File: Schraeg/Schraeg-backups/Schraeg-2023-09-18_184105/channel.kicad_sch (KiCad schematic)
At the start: 51 parts, among them U1 TL074, U2 TL074, U3 V2164, U4 TL074, U6 TL074

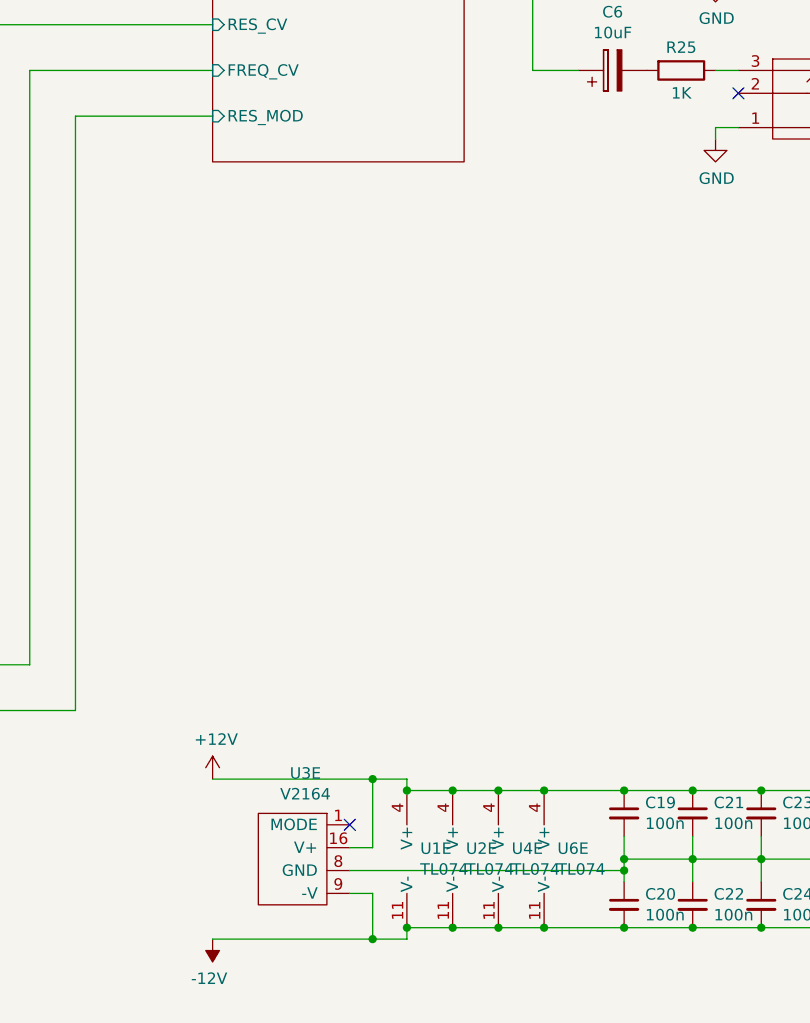
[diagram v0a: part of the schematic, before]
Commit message: fixes filter schematic
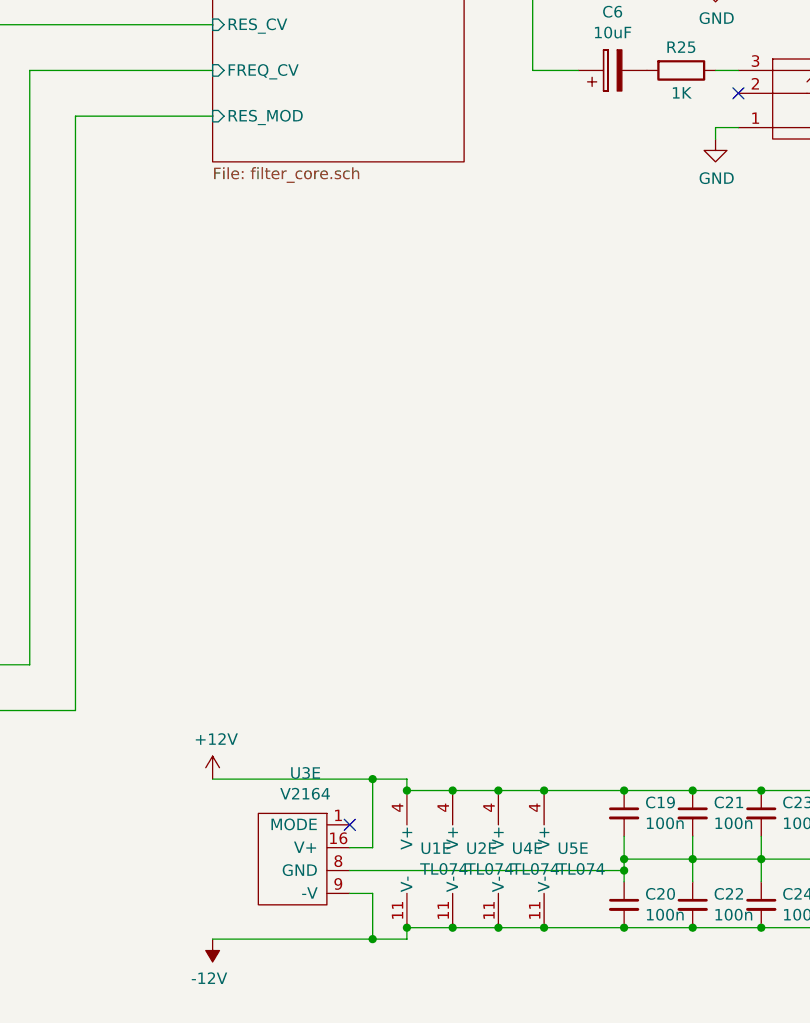
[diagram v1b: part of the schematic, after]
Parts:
- renumbered U6 to U5
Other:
- sheet Filter Core: file filter_core.kicad_sch -> filter_core.sch
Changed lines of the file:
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@@
   (symbol (lib_id "Device:C_Small") (at 110.49 107.95 0) (unit 1)
     (in_bom yes) (on_board yes) (dnp no)
-    (property "Reference" "C1" (at 112.8268 106.7816 0)
+    (property "Reference" "C?" (at 112.8268 106.7816 0)
       (effects (font (size 1.27 1.27)) (justify left))
     )
@@
   (symbol (lib_id "power:GND") (at 133.35 88.9 0) (unit 1)
     (in_bom yes) (on_board yes) (dnp no)
-    (property "Reference" "#PWR015" (at 133.35 95.25 0)
+    (property "Reference" "#PWR?" (at 133.35 95.25 0)
       (effects (font (size 1.27 1.27)) hide)
     )
@@
   (symbol (lib_id "power:GND") (at 110.49 110.49 0) (unit 1)
     (in_bom yes) (on_board yes) (dnp no)
-    (property "Reference" "#PWR013" (at 110.49 116.84 0)
+    (property "Reference" "#PWR?" (at 110.49 116.84 0)
       (effects (font (size 1.27 1.27)) hide)
     )
@@
   (symbol (lib_id "Schraeg-rescue:V2164-v2164") (at 120.65 97.79 0) (mirror x) (unit 1)
     (in_bom yes) (on_board yes) (dnp no)
-    (property "Reference" "U3" (at 121.285 89.789 0)
+    (property "Reference" "U?" (at 121.285 89.789 0)
       (effects (font (size 1.27 1.27)))
     )
@@
   (symbol (lib_id "power:GND") (at 110.49 77.47 180) (unit 1)
     (in_bom yes) (on_board yes) (dnp no)
-    (property "Reference" "#PWR012" (at 110.49 71.12 0)
+    (property "Reference" "#PWR?" (at 110.49 71.12 0)
       (effects (font (size 1.27 1.27)) hide)
     )
@@
   (symbol (lib_id "power:GND") (at 274.32 153.67 0) (unit 1)
     (in_bom yes) (on_board yes) (dnp no)
-    (property "Reference" "#PWR045" (at 274.32 160.02 0)
+    (property "Reference" "#PWR043" (at 274.32 160.02 0)
       (effects (font (size 1.27 1.27)) hide)
     )
@@
   (symbol (lib_id "Device:R") (at 110.49 101.6 180) (unit 1)
     (in_bom yes) (on_board yes) (dnp no)
-    (property "Reference" "R15" (at 112.268 100.4316 0)
+    (property "Reference" "R?" (at 112.268 100.4316 0)
       (effects (font (size 1.27 1.27)) (justify right))
     )
@@
   (symbol (lib_id "power:PWR_FLAG") (at 274.32 146.05 0) (unit 1)
     (in_bom yes) (on_board yes) (dnp no)
-    (property "Reference" "#FLG?" (at 274.32 144.145 0)
+    (property "Reference" "#FLG05" (at 274.32 144.145 0)
       (effects (font (size 1.27 1.27)) hide)
     )
@@
   (symbol (lib_id "Amplifier_Operational:TL074") (at 228.6 146.05 0) (unit 5)
     (in_bom yes) (on_board yes) (dnp no)
-    (property "Reference" "U6" (at 227.5332 144.8816 0)
+    (property "Reference" "U5" (at 227.5332 144.8816 0)
       (effects (font (size 1.27 1.27)) (justify left))
     )
@@
       (effects (font (size 1.27 1.27)) (justify left bottom))
     )
-    (property "Sheetfile" "filter_core.kicad_sch" (at 189.23 69.1646 0)
-      (effects (font (size 1.27 1.27)) (justify left top) hide)
+    (property "Sheetfile" "filter_core.sch" (at 189.23 69.1646 0)
+      (effects (font (size 1.27 1.27)) (justify left top))
     )
     (pin "AUDIO_IN" input (at 189.23 35.56 180)
@@
         (path "/63ba224f-cd90-44e3-9d07-b2fc4e2de32b" (page "2"))
         (path "/63ba224f-cd90-44e3-9d07-b2fc4e2de32b/4c523315-a660-4e97-96a6-b36e862376d0" (page "3"))
-        (path "/63ba224f-cd90-44e3-9d07-b2fc4e2de32b/77e223dd-0fbc-47b2-9b63-c429f2590121" (page "7"))
-      )
-    )
+        (path "/63ba224f-cd90-44e3-9d07-b2fc4e2de32b/77e223dd-0fbc-47b2-9b63-c429f2590121" (page "5"))
+      )
+    )
